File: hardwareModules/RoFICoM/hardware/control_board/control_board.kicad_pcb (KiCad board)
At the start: 2 copper layers, 48.5 x 48.5 mm, 51 parts, among them J1 Skirt Cable, J2 M+, J3 M-, J4 SWD, J5 DBG_UART, J6 SYS_CON, J7 SLIDER, J8 DBG, J9 SYS_CON_2, Q1 DMP6050SFG, Q2 SSM3K72CFS, Q3 DMP6050SFG, Q4 DMP6050SFG, Q5 SSM3K72CFS, Q6 DMP6050SFG, U1 STM32G071GBU6, U2 DRV8837C, U3 BU52272NUZ, U4 NCP718ASN330T1G, U5 BU52272NUZ, U6 ACS70331, U7 ACS70331

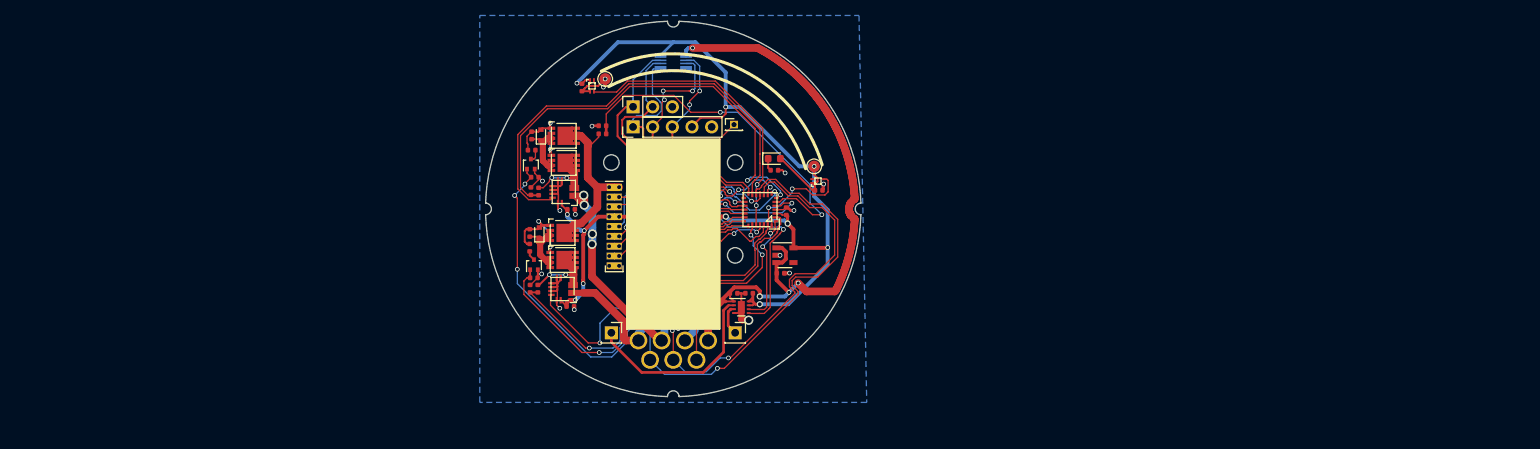
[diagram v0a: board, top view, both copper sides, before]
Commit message: universalModule: Prepare electronics v0.2
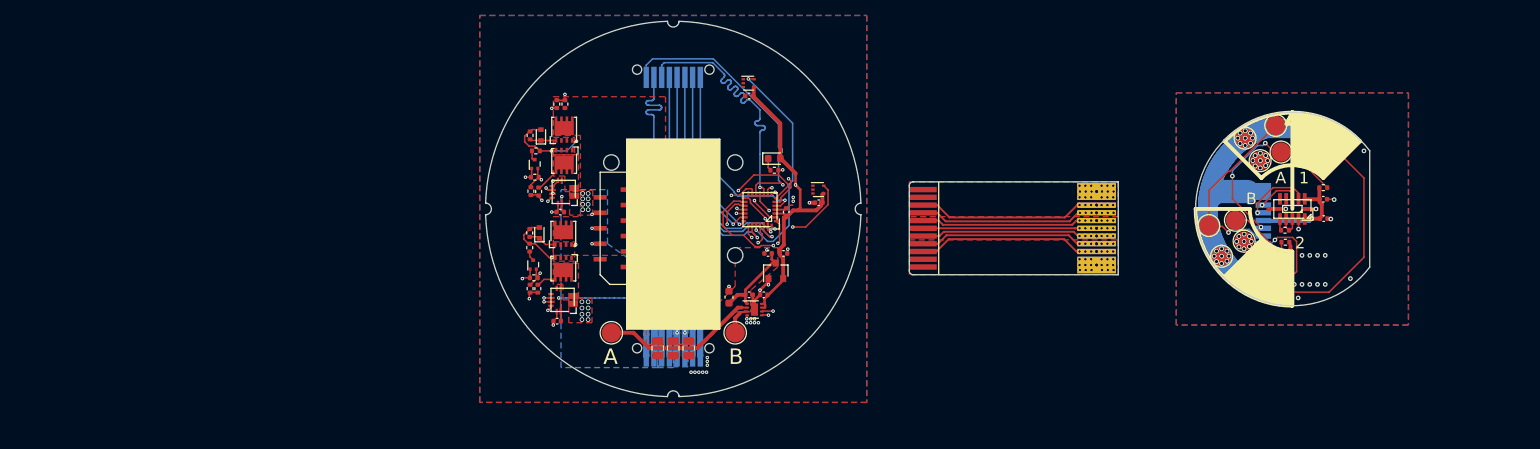
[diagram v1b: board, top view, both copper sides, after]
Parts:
- removed TP1, TP2: TestPoint, TestPoint:TestPoint_Pad_D1.5mm
- added BOARD1: BOARD, kikit:Board, F.Cu at (138.4, 65.8)
- added BOARD2: BOARD, kikit:Board, F.Cu at (220.0, 77.5)
- added BOARD3: BOARD, kikit:Board, F.Cu at (183.5, 98.5)
- added C10: 1u, Capacitor_SMD:C_0402_1005Metric, F.Cu at (158.8, 89.2)
- added C11: 22u, Capacitor_SMD:C_0805_2012Metric, F.Cu at (140.0, 108.0)
- added C12: 22u, Capacitor_SMD:C_0805_2012Metric, F.Cu at (142.0, 108.0)
- added C13: 22u, Capacitor_SMD:C_0805_2012Metric, F.Cu at (138.0, 108.0)
- added C14: 1u, Capacitor_SMD:C_0402_1005Metric, F.Cu at (224.1, 91.2)
- added C15: 100n, Capacitor_SMD:C_0402_1005Metric, F.Cu at (224.0, 88.8)
- added C9: 1u, Capacitor_SMD:C_0402_1005Metric, F.Cu at (149.8, 75.4)
- added J10: SENSE_A, rofi:pogo_pin_2mm, F.Cu at (218.5, 82.6)
- added J11: SENSE_B, rofi:pogo_pin_2mm, F.Cu at (212.6, 91.5)
- added J12: SENSE_1, rofi:pogo_pad_2mm, F.Cu at (221.5, 82.6)
- added J13: SENSE_2, rofi:pogo_pad_2mm, F.Cu at (218.5, 97.4)
- added J14: 48V_A, rofi:pogo_pin_2mm, F.Cu at (213.9, 80.9)
- added J15: 48V_1, rofi:pogo_pad_2mm, F.Cu at (213.9, 99.1)
- added J16: 48V_B, rofi:pogo_pin_2mm, F.Cu at (210.9, 96.1)
- added J17: 48V_2, rofi:pogo_pad_2mm, F.Cu at (226.1, 80.9)
- added J18: GND_A, rofi:pogo_pin_2mm, F.Cu at (215.8, 83.8)
- added J19: GND_1, rofi:pogo_pad_2mm, F.Cu at (224.2, 83.8)
- added J20: GND_B, rofi:pogo_pin_2mm, F.Cu at (213.8, 94.2)
- added J21: GND_2, rofi:pogo_pad_2mm, F.Cu at (215.8, 96.2)
- added J22: RX_A, rofi:pogo_pin_2mm, F.Cu at (209.2, 92.1)
- added J23: RX_B, rofi:pogo_pin_2mm, F.Cu at (217.9, 79.2)
- added J24: TX_1, rofi:pogo_pad_2mm, F.Cu at (222.1, 79.2)
- added J25: TX_2, rofi:pogo_pad_2mm, F.Cu at (217.9, 100.8)
- added R14: 100k, Resistor_SMD:R_0402_1005Metric, F.Cu at (219.1, 92.8)
- added R15: 6k8, Resistor_SMD:R_0402_1005Metric, F.Cu at (224.0, 87.2)
- added R16: 6k8, Resistor_SMD:R_0402_1005Metric, F.Cu at (219.1, 94.3)
- added U8: VL53L1X, rofi:VL53L1X_handsoldering, F.Cu at (220.0, 90.0)
- C1, C2, C3, C4, C5, C6, C7: value 470n -> 1u
- C8: value 470n -> 10u; footprint Capacitor_SMD:C_0402_1005Metric -> Capacitor_SMD:C_0603_1608Metric
- D2, D3: value 15V BZT52C15T-7 -> 15V EDZVT2R15B
- J1: value Skirt Cable -> BoardSkirtConnector; footprint rofi:flat_cable_9 -> rofi:FC38-11N1-AHK
- J2, J3: footprint Connector_PinSocket_2.54mm:PinSocket_1x01_P2.54mm_Vertical -> TestPoint:TestPoint_Pad_D2.5mm
- J4: value SWD -> SYS_CONN; footprint Connector_PinHeader_2.54mm:PinHeader_1x05_P2.54mm_Vertical -> rofi:SOLO-9258-mating; moved to B.Cu
- J5: value DBG_UART -> PWR_CONN_1; footprint Connector_PinSocket_2.54mm:PinSocket_1x03_P2.54mm_Vertical -> rofi:SOLO-9258-mating; moved to B.Cu
- J6: value SYS_CON -> PWR_CONN_2; footprint rofi:pogo_row_4_3 -> rofi:SOLO-9258-mating; moved to B.Cu
- J7: value SLIDER -> CableConnector; footprint Connector_PinHeader_1.27mm:PinHeader_1x01_P1.27mm_Vertical -> rofi:FPC_PADS_11
- J8: value DBG -> CablePads; footprint rofi:molex-505006-0812 -> rofi:RoFICoM_CableFPCPads; moved to F.Cu
- J9: value SYS_CON_2 -> SkirtPads; footprint rofi:molex-505006-0812 -> rofi:RoFICoM_CablePads
- Q1, Q3, Q4, Q6: value DMP6050SFG -> AONR21357; footprint rofi:POWERDI_3333-8 -> rofi:DFN3.3X3.3-EP
- Q2, Q5: value SSM3K72CFS -> PNM723T703E0-2; footprint Package_TO_SOT_SMD:SOT-416 -> Package_TO_SOT_SMD:SOT-723
- R1: value 220R -> 330R
- U3: value BU52272NUZ -> HX6306P332MR; footprint rofi:VSON04Z1114A -> Package_TO_SOT_SMD:SOT-23
- U4: value NCP718ASN330T1G -> KTH1611SH-SF5; footprint Package_TO_SOT_SMD:SOT-23-5 -> Package_TO_SOT_SMD:SOT-553
- U5: value BU52272NUZ -> KTH1611SH-SF5; footprint rofi:VSON04Z1114A -> Package_TO_SOT_SMD:SOT-553
- moved J9 76.8 mm to (216.2, 92.5), turned to 270 degrees
- moved J8 58.8 mm to (194.7, 92.5)
- moved C8 33.1 mm to (147.2, 101.4), turned to 270 degrees
- moved J5 31.6 mm to (140.0, 108.0), turned to 0 degrees
- moved J7 27.9 mm to (172.3, 92.5), turned to 270 degrees
- moved U5 20.3 mm to (149.8, 73.8)
- moved U3 12.8 mm to (153.2, 98.0)
- moved C4 12.5 mm to (154.6, 90.4), turned to 90 degrees
- moved C3 11.8 mm to (149.8, 101.1), turned to 180 degrees
- moved U4 9.52 mm to (158.8, 87.5)
- moved C2 9.33 mm to (154.2, 95.8), turned to 0 degrees
- moved J4 9.04 mm to (140.0, 72.0), turned to 0 degrees
- moved R13 6.53 mm to (125.0, 76.5), turned to 270 degrees
- moved R12 6.19 mm to (126.0, 76.5), turned to 90 degrees
- moved J6 5.00 mm to (140.0, 102.0)
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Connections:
- C2 pad 1: GND -> +3V3
- C2 pad 2: +3V3 -> GND
- C3 pad 1: +3V3 -> GND
- C3 pad 2: GND -> VCC
- C4 pad 1: GND -> +3V3
- C4 pad 2: VCC -> GND
- C8 pad 2: +3V3 -> VCC
- J1 pad 2: SENSE_B -> GND
- J1 pad 3: TX -> SENSE_B
- J1 pad 4: RX -> TX
- J1 pad 5: SENSE_A -> RX
- J1 pad 6: +3V3 -> SENSE_A
- J1 pad 7: SCL -> +3V3
- J1 pad 8: SDA -> SCL
- J1 pad 9: +48V -> SDA
- J4 pad 1: SWCLK -> SPI_MISO
- J4 pad 2: SWDIO -> SPI_SCK
- J4 pad 3: RST -> SPI_SS
- J4 pad 4: +3V3 -> DBG_TX
- J4 pad 5: GND -> DBG_RX
- J5 pad 1: DBG_TX -> EXT
- J5 pad 2: DBG_RX -> EXT
- J5 pad 3: GND -> INT
- J6 pad 2: INT -> EXT
- J6 pad 3: GND -> INT
- J6 pad 4: VCC -> INT
- J6 pad 5: SPI_MISO -> VCC
- J6 pad 6: SPI_SS -> VCC
- J6 pad 7: SPI_SCK -> GND
- J7 pad 1: POT_SENSE -> /C_48V
- J8 pad 1: VCC -> /C_GND
- J8 pad 2: +3V3 -> /C_SENSE_B
- J8 pad 3: RST -> /C_TX
- J8 pad 4: DBG_TX -> /C_RX
- J8 pad 5: SWDIO -> /C_SENSE_A
- J8 pad 6: DBG_RX -> /C_3V3
- J8 pad 7: GND -> /C_SCL
- J8 pad 8: SWCLK -> /C_SDA
- J9 pad 1: GND -> /skirt connector/48V
- J9 pad 2: VCC -> /skirt connector/SDA
- J9 pad 3: SPI_MISO -> /skirt connector/SCL
- J9 pad 4: SPI_SCK -> /skirt connector/3V3
- J9 pad 5: SPI_SS -> /skirt connector/S_A_PIN
- J9 pad 6: (no net) -> /skirt connector/RX
- J9 pad 7: INT -> /skirt connector/TX
- J9 pad 8: EXT -> /skirt connector/S_B_PIN
- Q1 pad 1: Net-(D2-Pad2) -> Net-(D2-Pad1)
- Q1 pad 2: Net-(D2-Pad1) -> Net-(D2-Pad2)
- Q3 pad 1: Net-(D2-Pad2) -> Net-(D2-Pad1)
- Q3 pad 2: Net-(D2-Pad1) -> Net-(D2-Pad2)
- Q4 pad 1: Net-(D3-Pad2) -> Net-(D3-Pad1)
- Q4 pad 2: Net-(D3-Pad1) -> Net-(D3-Pad2)
- Q6 pad 1: Net-(D3-Pad2) -> Net-(D3-Pad1)
- Q6 pad 2: Net-(D3-Pad1) -> Net-(D3-Pad2)
- U1 pad 14: POT_SENSE -> (no net)
- U3 pad 1: +3V3 -> GND
- U3 pad 2: GND -> +3V3
- U3 pad 3: LIMIT_2 -> VCC
- U4 pad 1: VCC -> (no net)
- U4 pad 3: VCC -> (no net)
- U4 pad 4: (no net) -> +3V3
- U4 pad 5: +3V3 -> LIMIT_2
- U5 pad 1: +3V3 -> (no net)
- U5 pad 3: LIMIT_1 -> (no net)
- U5 pad 4: (no net) -> +3V3
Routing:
- net VCC: track 87.8 -> 22.9 mm, vias 5 -> 8
- net +3V3: track 149.2 -> 94.5 mm, vias 11 -> 4
- net /skirt connector/TX: track 0.00 -> 46.2 mm, vias 0 -> 1
- net /skirt connector/48V: track 0.00 -> 41.4 mm, vias 0 -> 34
- net INT_SW: track 65.4 -> 37.0 mm, vias 4 -> 2
- net INT_I: track 57.4 -> 29.2 mm, vias 0 -> 2
- net +48V: track 26.1 -> 0.00 mm
- net SPI_MISO: track 61.8 -> 36.1 mm, vias 3 -> 1
- net /skirt connector/RX: track 0.00 -> 24.8 mm, vias 0 -> 1
- net DBG_RX: track 54.1 -> 29.8 mm, vias 2 -> 1
- net /C_SENSE_B: track 0.00 -> 23.8 mm, vias 0 -> 6
- net /C_SDA: track 0.00 -> 23.8 mm, vias 0 -> 6
- net /C_SCL: track 0.00 -> 23.5 mm, vias 0 -> 6
- net /C_TX: track 0.00 -> 23.4 mm, vias 0 -> 6
- net /C_RX: track 0.00 -> 22.9 mm, vias 0 -> 6
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- added copper zone on F.Cu, net +48V
- added copper zone on F.Cu, net /C_48V
- added copper zone on F.Cu, net /C_GND
- added copper zone on B.Cu, net /skirt connector/GND
- added copper zone on F.Cu, net /skirt connector/GND
- added copper zone on B.Cu, net EXT
- added copper zone on F.Cu, net EXT
- added copper zone on F.Cu, net GND
- added copper zone on In1.Cu, net GND
- added copper zone on In2.Cu, net GND
- added copper zone on B.Cu, net INT
- added copper zone on F.Cu, net INT
- added copper zone on F.Cu, net Net-(D2-Pad1)
- added copper zone on F.Cu, net Net-(D3-Pad1)
- added copper zone on F.Cu, net Net-(Q3-Pad3)
- added copper zone on F.Cu, net Net-(Q6-Pad3)
- added copper zone on B.Cu, net VCC
- added copper zone on F.Cu, net VCC
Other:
- board size 48.5 x 48.5 mm -> 114.2 x 48.5 mm
- copper layers 2 -> 4
- net class Default: via_dia 0.6 -> 0.8
- rule pad_to_mask_clearance: 0 -> 0.051
- rule trace_min: 0.15 -> 0.127
- rule via_min_drill: 0.3 -> 0.2
- rule via_min_size: 0.6 -> 0.45
- board text added: "1"
- board text added: "2"
- board text added: "A"
- board text added: "B"
- board text added: "Control Board v0.6 7/2021 ro.fi.muni.cz"
- board text added: "EXT INT VCC GND"
- board text added: "MISO MOSI SS TX RX SWIO SWCL RST"
- board text added: "RoFICoM Skirt v0.6 7/2021 ro.fi.muni.cz"
- board text removed: "CL SS IO"
- board text removed: "Control Board v0.5 8/2020 ro.fi.muni.cz"
- board text removed: "DBG"
- board text removed: "G RX TX"
- board text removed: "GND 3V3 RST IO CLK"
- board text removed: "INT EXT"
- board text removed: "RoFICoM"
- board text removed: "SWD"
- board text removed: "VCC GND"

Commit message: roficom: Implement v1 hardware
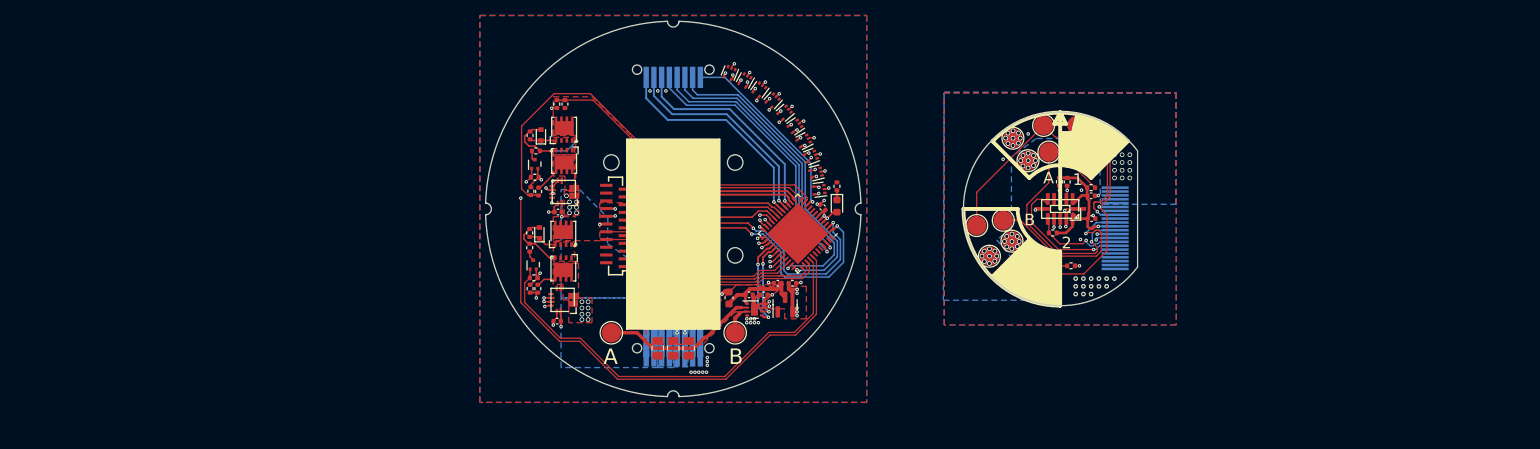
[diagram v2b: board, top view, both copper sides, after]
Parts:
- removed BOARD3: BOARD, kikit:Board
- removed C10, C9: 1u, Capacitor_SMD:C_0402_1005Metric
- removed J7: CableConnector, rofi:FPC_PADS_11
- removed J8: CablePads, rofi:RoFICoM_CableFPCPads
- removed J9: SkirtPads, rofi:RoFICoM_CablePads
- removed U1: STM32G071GBU6, rofi:UFQFPN28
- removed U4, U5: KTH1611SH-SF5, Package_TO_SOT_SMD:SOT-553
- added HAL1: KTH1611SH-SF5, Package_TO_SOT_SMD:SOT-553, F.Cu at (147.3, 72.4)
- added HAL10: KTH1611SH-SF5, Package_TO_SOT_SMD:SOT-553, F.Cu at (158.8, 87.5)
- added HAL2: KTH1611SH-SF5, Package_TO_SOT_SMD:SOT-553, F.Cu at (149.3, 73.4)
- added HAL3: KTH1611SH-SF5, Package_TO_SOT_SMD:SOT-553, F.Cu at (151.1, 74.6)
- added HAL4: KTH1611SH-SF5, Package_TO_SOT_SMD:SOT-553, F.Cu at (152.8, 76.0)
- added HAL5: KTH1611SH-SF5, Package_TO_SOT_SMD:SOT-553, F.Cu at (154.4, 77.6)
- added HAL6: KTH1611SH-SF5, Package_TO_SOT_SMD:SOT-553, F.Cu at (155.7, 79.3)
- added HAL7: KTH1611SH-SF5, Package_TO_SOT_SMD:SOT-553, F.Cu at (156.9, 81.2)
- added HAL8: KTH1611SH-SF5, Package_TO_SOT_SMD:SOT-553, F.Cu at (157.8, 83.2)
- added HAL9: KTH1611SH-SF5, Package_TO_SOT_SMD:SOT-553, F.Cu at (158.4, 85.3)
- added J26: BoardSkirtConnector, rofi:781272210, F.Cu at (132.5, 92.2)
- added R17: 6k8, Resistor_SMD:R_0402_1005Metric, F.Cu at (190.9, 86.5)
- added R18: 6k8, Resistor_SMD:R_0402_1005Metric, F.Cu at (189.9, 86.5)
- added U9: STM32G071CBUx, Package_DFN_QFN:QFN-48-1EP_7x7mm_P0.5mm_EP5.6x5.6mm, F.Cu at (156.1, 93.2)
- J1: value BoardSkirtConnector -> SkirtConnector; footprint rofi:FC38-11N1-AHK -> rofi:FPC_0.5_22_PADS; moved to B.Cu
- moved J1 64.8 mm to (197.1, 92.5)
- moved C15 30.0 mm to (194.0, 88.3)
- moved R14 30.0 mm to (189.1, 93.1)
- moved BOARD2 30.0 mm to (190.0, 77.5)
- moved C14 30.0 mm to (194.1, 91.2)
- moved J10 30.0 mm to (188.5, 82.6)
- moved J11 30.0 mm to (182.6, 91.5)
- moved J12 30.0 mm to (191.5, 82.6)
- moved J13 30.0 mm to (188.5, 97.4)
- moved J14 30.0 mm to (183.9, 80.9)
- moved J15 30.0 mm to (183.9, 99.1)
- moved J16 30.0 mm to (180.9, 96.1)
- moved J17 30.0 mm to (196.1, 80.9)
- moved J18 30.0 mm to (185.8, 83.8)
- moved J19 30.0 mm to (194.2, 83.8)
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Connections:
- J1 pad 1: GND -> /skirt connector/GND
- J1 pad 10: +48V -> /skirt connector/SCL
- J1 pad 11: +48V -> /skirt connector/S_A_PIN
- J1 pad 2: GND -> /skirt connector/GND
- J1 pad 3: SENSE_B -> /skirt connector/GND
- J1 pad 4: TX -> /skirt connector/GND
- J1 pad 5: RX -> /skirt connector/GND
- J1 pad 6: SENSE_A -> /skirt connector/GND
- J1 pad 7: +3V3 -> /skirt connector/IRQ
- J1 pad 8: SCL -> /skirt connector/EN
- J1 pad 9: SDA -> /skirt connector/SDA
- R14 pad 1: Net-(R14-Pad1) -> /skirt connector/EN
- R14 pad 2: /skirt connector/GND -> /skirt connector/3V3
- U8 pad 5: Net-(R14-Pad1) -> /skirt connector/EN
- U8 pad 7: (no net) -> /skirt connector/IRQ
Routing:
- net +3V3: track 94.5 -> 28.0 mm, vias 4 -> 23
- net /skirt connector/48V: track 41.4 -> 0.00 mm, vias 34 -> 48
- net INT_SW: track 37.0 -> 71.3 mm
- net LIDAR_EN: track 0.00 -> 30.9 mm
- net LIDAR_IRQ: track 0.00 -> 29.4 mm
- net LIMIT_1: track 28.6 -> 0.00 mm, vias 2 -> 0
- net /POS1: track 0.00 -> 24.1 mm, vias 0 -> 2
- net /C_SENSE_B: track 23.8 -> 0.00 mm, vias 6 -> 0
- net /C_SDA: track 23.8 -> 0.00 mm, vias 6 -> 0
- net /C_SCL: track 23.5 -> 0.00 mm, vias 6 -> 0
- net /C_TX: track 23.4 -> 0.00 mm, vias 6 -> 0
- net /C_RX: track 22.9 -> 0.00 mm, vias 6 -> 0
- net /C_3V3: track 22.9 -> 0.00 mm, vias 6 -> 0
- net /C_SENSE_A: track 22.4 -> 0.00 mm, vias 6 -> 0
- net /POS2: track 0.00 -> 22.1 mm, vias 0 -> 2
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- added copper zone on F.Cu, net +3V3
- added copper zone on In1.Cu, net +3V3
- added copper zone on B.Cu, net /skirt connector/48V
- added copper zone on In1.Cu, net /skirt connector/48V
- added copper zone on In2.Cu, net /skirt connector/GND
- removed copper zone on F.Cu, net /C_48V
- removed copper zone on F.Cu, net /C_GND
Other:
- board size 114.2 x 48.5 mm -> 84.2 x 48.5 mm
- net class Default removed
- board text added: "Control Board v1.0 2/2023 ro.fi.muni.cz"
- board text added: "RoFICoM Skirt v1.0 2/2023 ro.fi.muni.cz"
- board text removed: "Control Board v0.6 7/2021 ro.fi.muni.cz"
- board text removed: "RoFICoM Skirt v0.6 7/2021 ro.fi.muni.cz"

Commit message: hardware: Add custom FPC cables
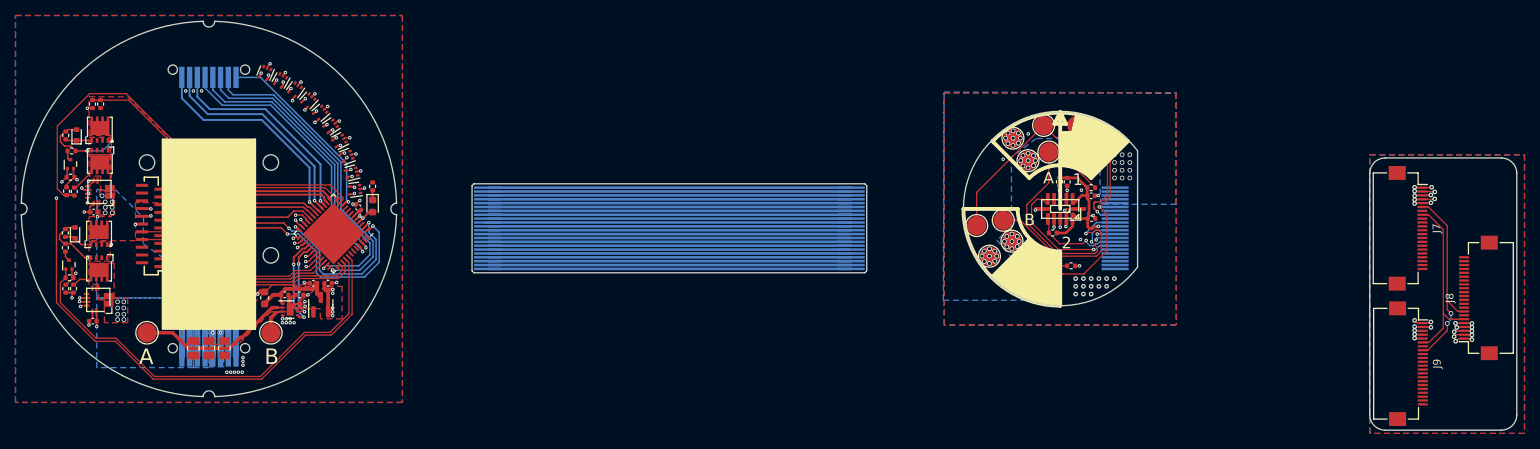
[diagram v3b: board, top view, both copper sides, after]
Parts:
- added BOARD3: BOARD, kikit:Board, F.Cu at (247.0, 83.4)
- added BOARD4: BOARD, kikit:Board, F.Cu at (144.8, 86.8)
- added J27: SkirtConnector, rofi:FPC_0.5_22_PADS, B.Cu at (116.0, 92.5)
- added J28: SkirtConnector, rofi:FPC_0.5_22_PADS, B.Cu at (163.0, 92.5)
- added J7: SIDE_1, Connector_FFC-FPC:Hirose_FH12-22S-0.5SH_1x22-1MP_P0.50mm_Horizontal, F.Cu at (234.9, 92.5)
- added J8: SIDE_2, Connector_FFC-FPC:Hirose_FH12-22S-0.5SH_1x22-1MP_P0.50mm_Horizontal, F.Cu at (244.1, 101.5)
- added J9: SIDE_3, Connector_FFC-FPC:Hirose_FH12-22S-0.5SH_1x22-1MP_P0.50mm_Horizontal, F.Cu at (235.0, 110.0)
- Q1, Q3, Q4, Q6: value AONR21357 -> AP20P30Q
- moved C3 60.0 mm to (89.8, 101.1)
- moved C4 60.0 mm to (99.3, 89.8)
- moved HAL10 60.0 mm to (98.8, 87.5)
- moved D2 60.0 mm to (62.9, 80.5)
- moved Q5 60.0 mm to (61.9, 97.2)
- moved BOARD1 60.0 mm to (78.4, 65.8)
- moved C1 60.0 mm to (93.5, 99.6)
- moved C11 60.0 mm to (80.0, 108.0)
- moved C12 60.0 mm to (82.0, 108.0)
- moved C13 60.0 mm to (78.0, 108.0)
- moved C2 60.0 mm to (95.4, 99.6)
- moved C6 60.0 mm to (65.1, 90.4)
- moved C7 60.0 mm to (65.0, 104.5)
- moved D1 60.0 mm to (101.2, 89.6)
- moved D3 60.0 mm to (62.7, 93.1)
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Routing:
- net Net-(J27-Pin_13): track 0.00 -> 47.3 mm
- net Net-(J27-Pin_9): track 0.00 -> 46.9 mm
- net Net-(J27-Pin_8): track 0.00 -> 46.9 mm
- net Net-(J27-Pin_7): track 0.00 -> 46.9 mm
- net Net-(J27-Pin_5): track 0.00 -> 46.9 mm
- net Net-(J27-Pin_4): track 0.00 -> 46.9 mm
- net Net-(J27-Pin_3): track 0.00 -> 46.9 mm
- net Net-(J27-Pin_22): track 0.00 -> 46.9 mm
- net Net-(J27-Pin_21): track 0.00 -> 46.9 mm
- net Net-(J27-Pin_2): track 0.00 -> 46.9 mm
- net Net-(J27-Pin_19): track 0.00 -> 46.9 mm
- net Net-(J27-Pin_18): track 0.00 -> 46.9 mm
- net Net-(J27-Pin_17): track 0.00 -> 46.9 mm
- net Net-(J27-Pin_16): track 0.00 -> 46.9 mm
- net Net-(J27-Pin_15): track 0.00 -> 46.9 mm
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- added copper zone on B.Cu, net /DbgCable/48V
- added copper zone on F.Cu, net /DbgCable/GND
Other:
- board size 84.2 x 48.5 mm -> 193.2 x 52.8 mm
- board text added: "RoFICoM Cable v1.0 4/2023 ro.fi.muni.cz"
- board text added: "RoFICoM Interconnector v1.0 3/2023 ro.fi.muni.cz"
- board text added: "RoFICoM Skirt v1.1 4/2023 ro.fi.muni.cz"
- board text removed: "RoFICoM Skirt v1.0 2/2023 ro.fi.muni.cz"

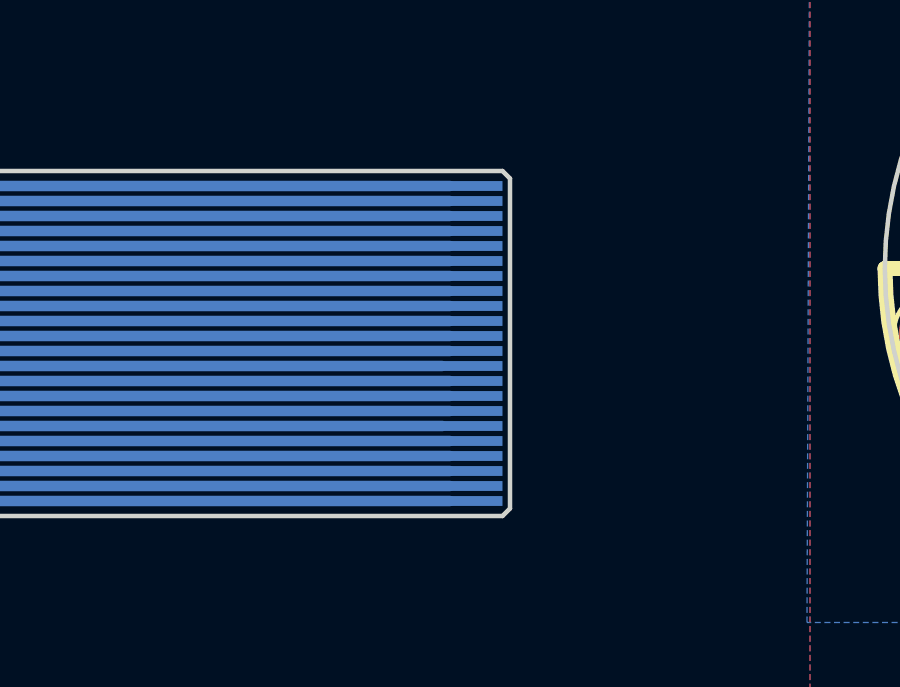
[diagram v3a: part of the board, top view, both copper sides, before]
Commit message: hardware: Update FPC cables
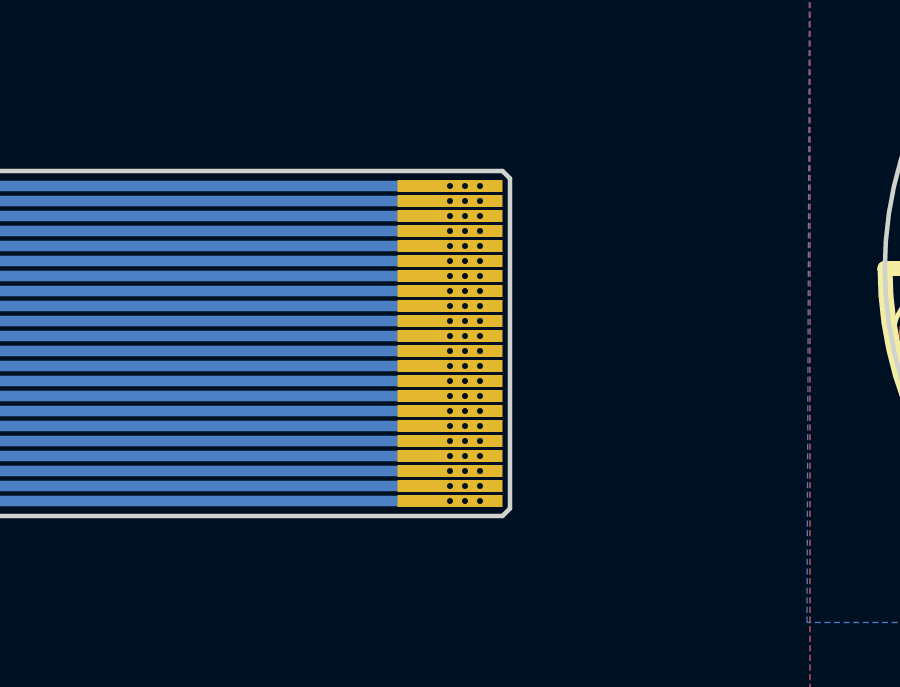
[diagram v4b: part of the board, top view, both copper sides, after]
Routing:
- net Net-(J27-Pin_9): vias 0 -> 2
- net Net-(J27-Pin_8): vias 0 -> 2
- net Net-(J27-Pin_7): vias 0 -> 2
- net Net-(J27-Pin_6): vias 0 -> 2
- net Net-(J27-Pin_5): vias 0 -> 2
- net Net-(J27-Pin_4): vias 0 -> 2
- net Net-(J27-Pin_3): vias 0 -> 2
- net Net-(J27-Pin_22): vias 0 -> 2
- net Net-(J27-Pin_21): vias 0 -> 2
- net Net-(J27-Pin_20): vias 0 -> 2
- net Net-(J27-Pin_2): vias 0 -> 2
- net Net-(J27-Pin_19): vias 0 -> 2
- net Net-(J27-Pin_18): vias 0 -> 2
- net Net-(J27-Pin_17): vias 0 -> 2
- net Net-(J27-Pin_16): vias 0 -> 2
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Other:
- board text added: "RoFICoM Cable v1.1 9/2023 ro.fi.muni.cz"
- board text removed: "RoFICoM Cable v1.0 4/2023 ro.fi.muni.cz"
